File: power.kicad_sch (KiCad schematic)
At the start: 13 parts, among them J2 Conn_01x04_Socket, SW1 Push_button, U20 MIC1232

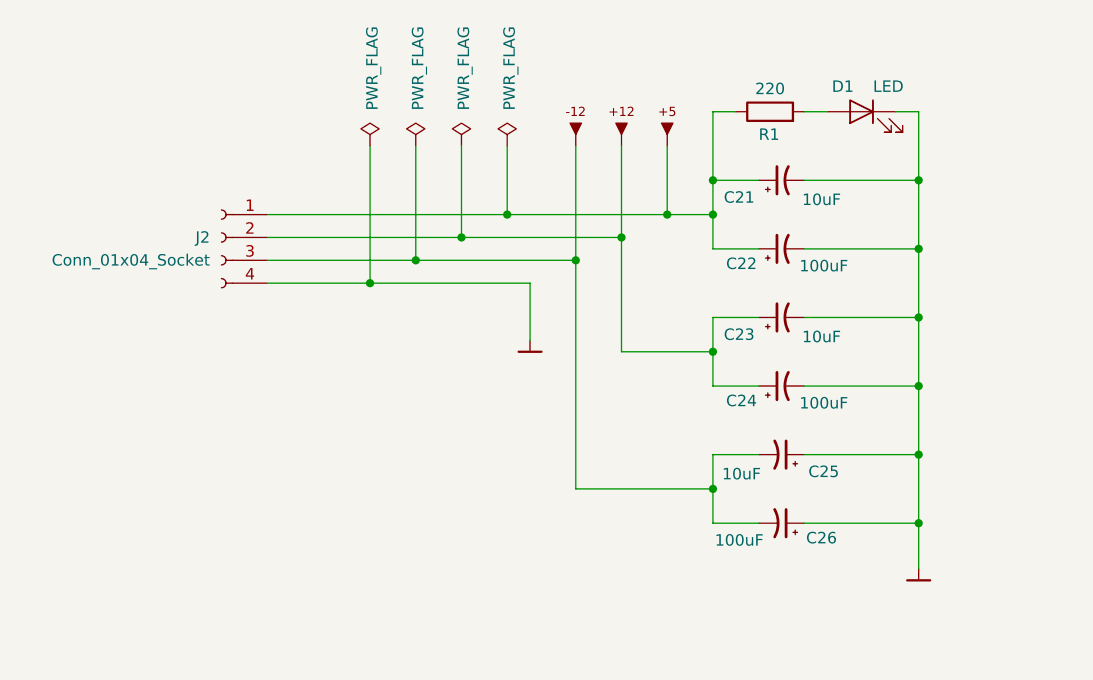
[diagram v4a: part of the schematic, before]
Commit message: Resolve power connector pinout
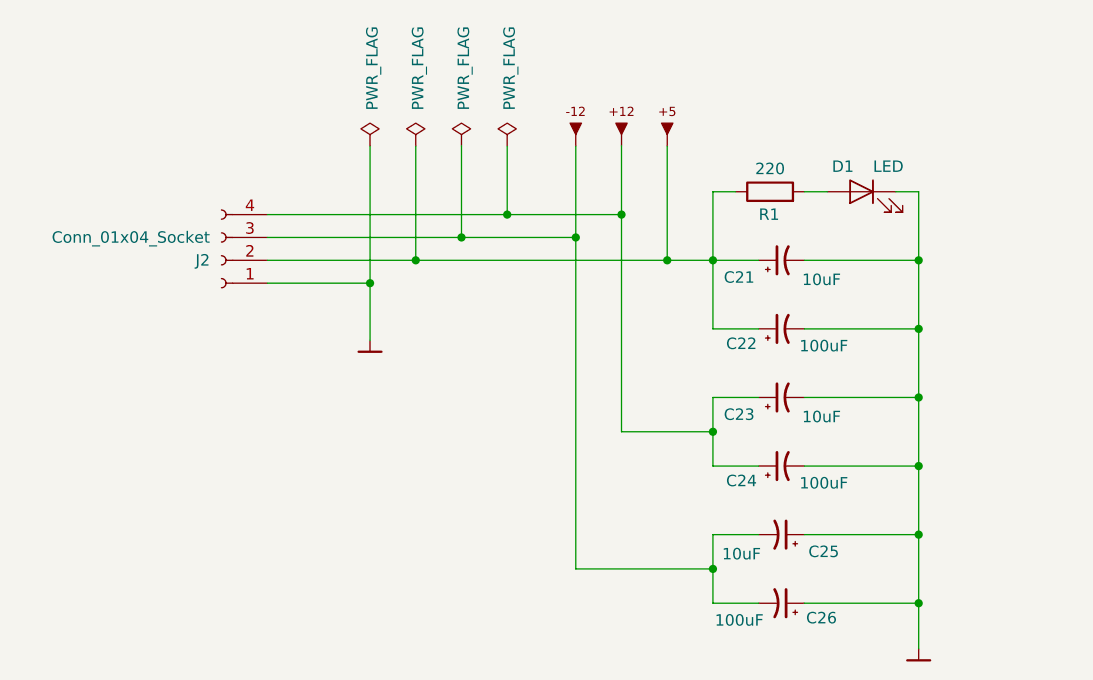
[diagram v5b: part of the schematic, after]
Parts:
- J2: footprint (none) -> PCM_artemisa:JST_XH-4
- U20: footprint (none) -> PCM_artemisa:DIP-8_300
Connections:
- net 12V: now also J2.4 (Pin_4); no longer J2.2 (Pin_2)
- net GND: now also J2.1 (Pin_1); no longer J2.4 (Pin_4)
- net VCC: now also J2.2 (Pin_2); no longer J2.1 (Pin_1)
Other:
- moved on the sheet: C21, C22, C23, C24, C25, C26, D1, J2, R1

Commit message: Adjust footprints and draft PCB layout
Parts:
- C21, C23, C25: footprint PCM_artemisa:Radial_capacitor -> Capacitor_THT:CP_Radial_D4.0mm_P2.00mm
- C22, C24, C26: footprint PCM_artemisa:Radial_capacitor -> Capacitor_THT:CP_Radial_D5.0mm_P2.50mm
- C27: footprint PCM_artemisa:Disc_capacitor -> Capacitor_THT:C_Disc_D5.0mm_W2.5mm_P2.50mm
- D1: footprint PCM_artemisa:LED -> Connector_PinHeader_2.54mm:PinHeader_1x02_P2.54mm_Vertical
- J2: footprint PCM_artemisa:JST_XH-4 -> Connector_JST:JST_XH_B4B-XH-A_1x04_P2.50mm_Vertical
- R1, R2: footprint PCM_artemisa:Axial_resistor -> Resistor_THT:R_Axial_DIN0207_L6.3mm_D2.5mm_P10.16mm_Horizontal
- U20: footprint PCM_artemisa:DIP-8_300 -> Package_DIP:DIP-8_W7.62mm
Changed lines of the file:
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@@
 			)
 		)
-		(property "Footprint" "PCM_artemisa:DIP-8_300"
+		(property "Footprint" "Package_DIP:DIP-8_W7.62mm"
 			(at 209.55 92.71 0)
 			(hide yes)
@@
 			)
 		)
-		(property "Footprint" "PCM_artemisa:Disc_capacitor"
+		(property "Footprint" "Capacitor_THT:C_Disc_D5.0mm_W2.5mm_P2.50mm"
 			(at 217.17 71.12 0)
 			(hide yes)
@@
 			)
 		)
-		(property "Footprint" "PCM_artemisa:JST_XH-4"
+		(property "Footprint" "Connector_JST:JST_XH_B4B-XH-A_1x04_P2.50mm_Vertical"
 			(at 49.53 85.09 0)
 			(hide yes)
@@
 			)
 		)
-		(property "Footprint" "PCM_artemisa:Radial_capacitor"
+		(property "Footprint" "Capacitor_THT:CP_Radial_D5.0mm_P2.50mm"
 			(at 111.76 107.95 0)
 			(hide yes)
@@
 			)
 		)
-		(property "Footprint" "PCM_artemisa:Radial_capacitor"
+		(property "Footprint" "Capacitor_THT:CP_Radial_D5.0mm_P2.50mm"
 			(at 111.76 123.19 0)
 			(hide yes)
@@
 			)
 		)
-		(property "Footprint" "PCM_artemisa:Radial_capacitor"
+		(property "Footprint" "Capacitor_THT:CP_Radial_D5.0mm_P2.50mm"
 			(at 111.76 92.71 0)
 			(hide yes)
@@
 			)
 		)
-		(property "Footprint" "PCM_artemisa:Axial_resistor"
+		(property "Footprint" "Resistor_THT:R_Axial_DIN0207_L6.3mm_D2.5mm_P10.16mm_Horizontal"
 			(at 233.68 80.01 0)
 			(hide yes)
@@
 			)
 		)
-		(property "Footprint" "PCM_artemisa:Radial_capacitor"
+		(property "Footprint" "Capacitor_THT:CP_Radial_D4.0mm_P2.00mm"
 			(at 111.76 85.09 0)
 			(hide yes)
@@
 			)
 		)
-		(property "Footprint" "PCM_artemisa:Radial_capacitor"
+		(property "Footprint" "Capacitor_THT:CP_Radial_D4.0mm_P2.00mm"
 			(at 111.76 100.33 0)
 			(hide yes)
@@
 			)
 		)
-		(property "Footprint" "PCM_artemisa:LED"
+		(property "Footprint" "Connector_PinHeader_2.54mm:PinHeader_1x02_P2.54mm_Vertical"
 			(at 120.65 77.47 0)
 			(hide yes)
@@
 			)
 		)
-		(property "Footprint" "PCM_artemisa:Radial_capacitor"
+		(property "Footprint" "Capacitor_THT:CP_Radial_D4.0mm_P2.00mm"
 			(at 111.76 115.57 0)
 			(hide yes)
@@
 			)
 		)
-		(property "Footprint" "PCM_artemisa:Axial_resistor"
+		(property "Footprint" "Resistor_THT:R_Axial_DIN0207_L6.3mm_D2.5mm_P10.16mm_Horizontal"
 			(at 110.49 77.47 90)
 			(hide yes)
